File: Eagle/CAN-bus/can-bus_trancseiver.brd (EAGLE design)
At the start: 53 x 32 mm, 10 parts

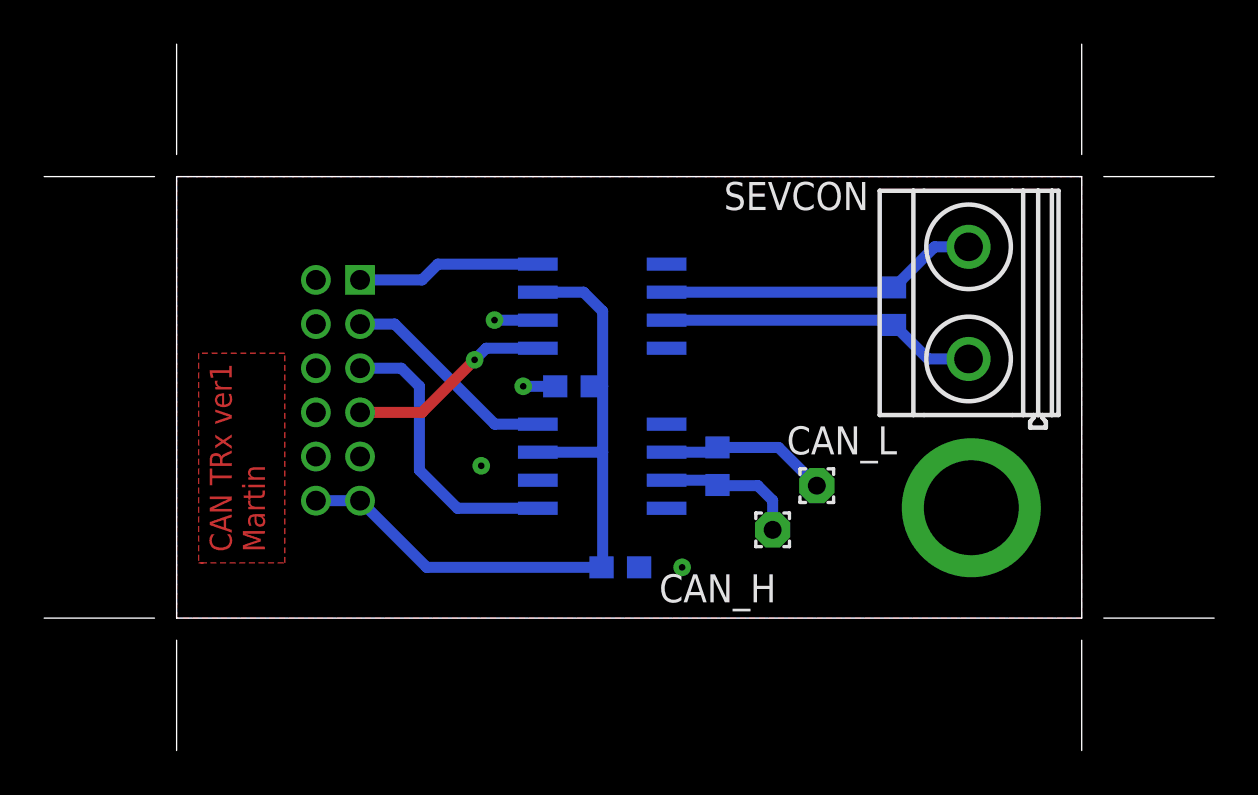
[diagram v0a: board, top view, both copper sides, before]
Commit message: Had to change resistor and capacitor packages to 0805
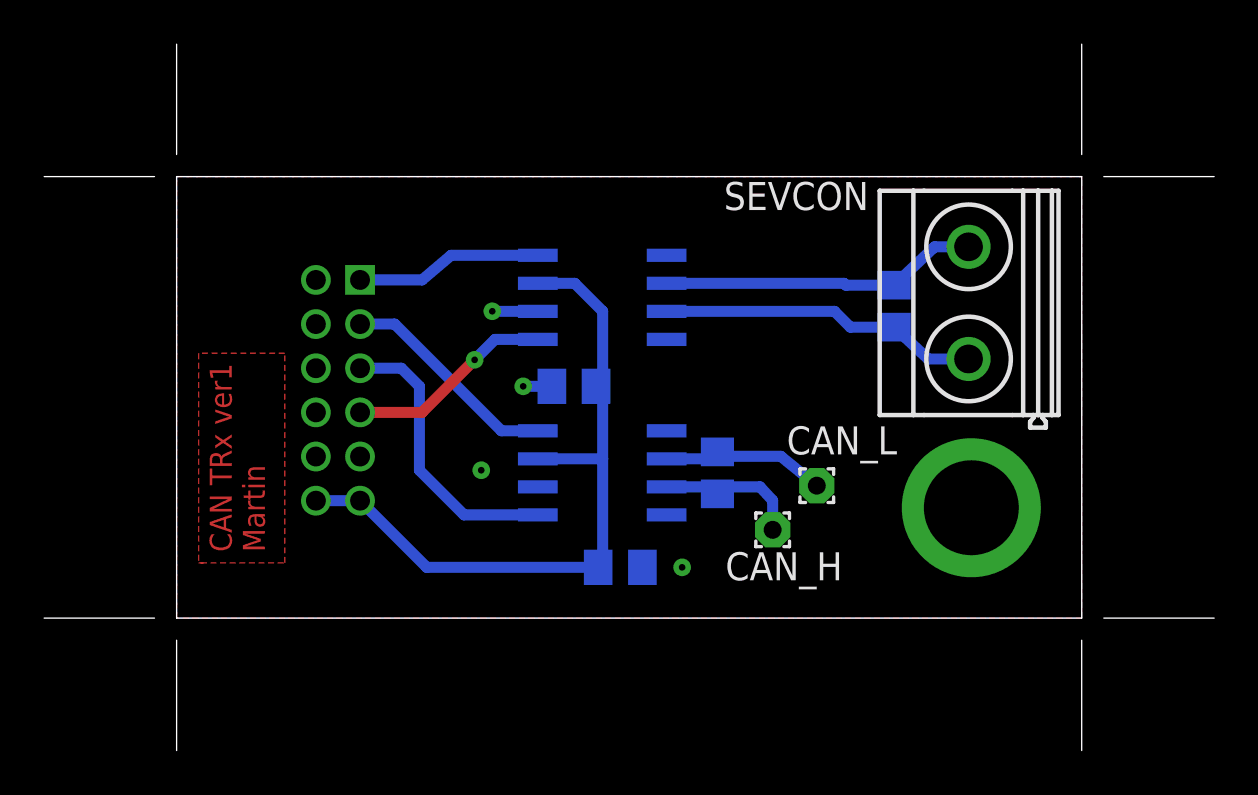
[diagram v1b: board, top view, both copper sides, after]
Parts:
- C0, C1: device rcl:C0603 -> rcl:C0805K
- R0, R1: device rcl:R0603 -> rcl:R0805
- moved CAN1 0.40 mm to (19.3, 14.5)
- moved CAN0 0.30 mm to (19.3, 6.58)
- moved R0 0.30 mm to (24.5, 6.58)
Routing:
- net N$9: track 14.4 -> 14.9 mm

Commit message: Second attempt to create a PCB
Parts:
- ZYBO: device PERSONAL:PMOD -> PERSONAL:PMOD12
- moved CAN_H 1.41 mm to (28.0, 3.00)
- moved CAN_L 1.41 mm to (30.0, 5.00)
- moved ZYBO 1.36 mm to (7.21, 11.7), flipped to the top, turned to 270 degrees
- moved R0 1.00 mm to (25.5, 6.58)
- moved R1 0.08 mm to (32.5, 14.2)
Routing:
- net N$3: track 10.1 -> 13.1 mm
- net N$12: track 7.53 -> 9.90 mm
- net N$8: track 6.86 -> 8.86 mm
- net N$2: track 13.0 -> 14.4 mm
- net N$4: track 9.42 -> 8.80 mm

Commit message: a
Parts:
- SEVCON: value MKDSN1,5/2-5,08 -> 2-5,08mm
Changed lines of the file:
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@@
 <attribute name="NAME" x="18.225" y="2.595" size="1.016" layer="26" ratio="18" rot="MR0"/>
 </element>
-<element name="SEVCON" library="con-phoenix-508" package="MKDSN1,5/2-5,08" value="MKDSN1,5/2-5,08" x="35.9" y="14.3" smashed="yes" rot="R90">
+<element name="SEVCON" library="con-phoenix-508" package="MKDSN1,5/2-5,08" value="2-5,08mm" x="35.9" y="14.3" smashed="yes" rot="R90">
 <attribute name="NAME" x="31.3511" y="19.755" size="1.27" layer="25" rot="R180"/>
 </element>
